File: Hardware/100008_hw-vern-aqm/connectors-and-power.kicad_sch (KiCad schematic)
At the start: 25 parts

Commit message: schematic work
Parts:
- removed D? (x2): ESD321, Diode_SMD:D_SOD-523, symbol Diode:ESD5Zxx
- added D? (x4): ESD321DYAR, Diode_SMD:D_SOD-523, symbol Active-Components:ESD321DYAR
- added R? (x2): 100R, Resistor_SMD:R_0603_1608Metric, symbol Device:R
- R?: now not fitted; now left out of the parts list
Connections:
- net GND: now also D?.2 (A), D?.2 (A), D?.2 (A), D?.2 (A)
- net UART0_RX: now also R?.2; no longer J?.2 (Pin_2)
- net UART0_TX: now also R?.2; no longer J?.1 (Pin_1)
- net at J?.A7 (D-), J?.B7 (D-), R?.1: now also D?.1 (K)
- net at J?.A6 (D+), J?.B6 (D+), R?.1: now also D?.1 (K)
- new net: D?.1 (K), J?.1 (Pin_1), R?.1
- new net: D?.1 (K), J?.2 (Pin_2), R?.1
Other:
- moved on the sheet: C?, D?, F?, J?, R?, U?

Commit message: schematic work
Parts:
- removed D?: LED, LED_SMD:LED_0805_2012Metric, symbol Device:LED
- removed J?: USB_C_Receptacle_USB2.0_16P, symbol Connector:USB_C_Receptacle_USB2.0_16P
- added D?: LED, LED_SMD:LED_0603_1608Metric, symbol Device:LED
- added J?: USB4220-03-1000-C, Mechanical:USB_C_Receptacle_GCT_USB4220-03-xxxx-C_Vertical, symbol Mechanical-Parts:GCT_USB4220-03-1000-C
- added TP? (x2): TestPoint, TestPoint:TestPoint_Pad_D1.5mm, symbol Connector:TestPoint
- D?: footprint LED_SMD:LED_0805_2012Metric -> LED_SMD:LED_0603_1608Metric
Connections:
- net +3V3: now also TP?.1
- net GND: now also D?.1 (K), J?.A1 (GND), J?.A12 (GND), J?.B1 (GND), J?.B12 (GND), J?.S1 (SHIELD)
- net VBUS: now also TP?.1
- net at R?.2: now also D?.2 (A)
- net at R?.1: now also J?.B5 (CC2)
- net at D?.1 (K), R?.1: now also J?.A7 (D-), J?.B7 (D-)
- net at D?.1 (K), R?.1: now also J?.A6 (D+), J?.B6 (D+)
- net at D?.1 (K), F?.1: now also J?.A4 (VBUS), J?.A9 (VBUS), J?.B4 (VBUS), J?.B9 (VBUS)
- net at R?.1: now also J?.A5 (CC1)
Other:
- moved on the sheet: C?, D?, F?, J?, R?, U?

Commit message: schematic work
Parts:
- added C? (x2): 10u, Capacitor_SMD:C_0805_2012Metric, symbol Device:C
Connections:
- net +3V3: now also C?.1
- net GND: now also C?.2, C?.2
- net VBUS: now also C?.1
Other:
- moved on the sheet: C?, R?, U?

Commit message: schematic and pcb work
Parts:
- added J?: Conn_01x04_Socket, symbol Connector:Conn_01x04_Socket
- added R? (x3): 10k, Resistor_SMD:R_0603_1608Metric, symbol Device:R
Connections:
- net +3V3: now also R?.1, R?.1, R?.1
- net GND: now also J?.MP (MountPin)
- new net SD_CS(D3): J?.1 (Pin_1), R?.2
- new net SD_MISO(D0): J?.3 (Pin_3), R?.2
- new net SD_MOSI(CMD): J?.2 (Pin_2), R?.2
- new net SD_SCK(CLK): J?.4 (Pin_4)
- no-connect marks 6 -> 5
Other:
- note added: "LCD Display SD card pin header connector"
- moved on the sheet: D?, J?, R?, TP?

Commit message: schematic and pcb layout
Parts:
- added J5: Conn_01x06_Socket, Connector_PinHeader_2.00mm:PinHeader_1x06_P2.00mm_Vertical, symbol Connector:Conn_01x06_Socket
- added J7: Conn_01x05_Pin, Connector_PinHeader_2.54mm:PinHeader_1x05_P2.54mm_Vertical, symbol Connector:Conn_01x05_Pin
- added R10: 0R0, Resistor_SMD:R_0603_1608Metric, symbol Device:R
- C2: renamed from C?; now not fitted
- F1: renamed from F?; footprint (none) -> Fuse:Fuse_1206_3216Metric; MFN (none) -> SN050-08
- J1: renamed from J?; footprint (none) -> Connector_PinHeader_2.54mm:PinHeader_1x14_P2.54mm_Vertical
- J4: renamed from J?; footprint (none) -> Connector_PinHeader_2.54mm:PinHeader_1x03_P2.54mm_Vertical
- J6: renamed from J?; footprint (none) -> Connector_PinHeader_2.54mm:PinHeader_1x04_P2.54mm_Vertical
- gave numbers to parts that had none: 32
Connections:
- net +3V3: no longer C5.1, C6.1
- net GND: now also J5.2 (Pin_2), J7.5 (Pin_5), R10.2
- net I2C_SCL: now also J5.4 (Pin_4)
- net I2C_SDA: now also J5.3 (Pin_3)
- net VBUS: now also J5.1 (Pin_1)
- net at R14.1, U1.2 (VO): now also C5.1, C6.1
- new net: J5.5 (Pin_5), R10.1
- new net JTAG_TCK: J7.1 (Pin_1)
- new net JTAG_TDI: J7.3 (Pin_3)
- new net JTAG_TDO: J7.2 (Pin_2)
- new net JTAG_TMS: J7.4 (Pin_4)
- no-connect marks 5 -> 6
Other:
- note added: "JTAG connector"
- moved on the sheet: C5, C6, D4, D5, D6, D7, R14, R15, R16, TP1, TP2

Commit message: schematic and pcb general layout
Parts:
- added H1, H2, H3, H4: MountingHole, MountingHole:MountingHole_4.5mm, symbol Mechanical:MountingHole
- J1, J6: now not fitted
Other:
- note added: "Mounting holes"

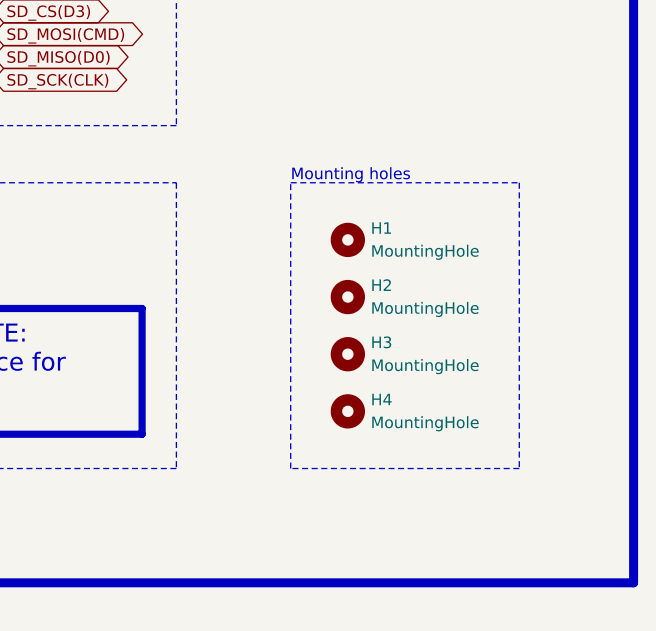
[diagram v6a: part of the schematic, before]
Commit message: schematic, pcb layout, added mouser shoping cart
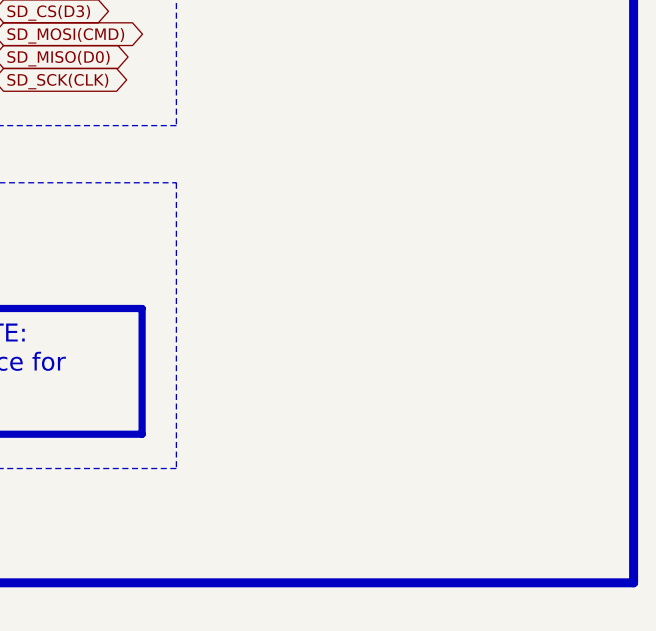
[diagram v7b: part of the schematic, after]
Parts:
- removed H1, H2, H3, H4: MountingHole, MountingHole:MountingHole_4.5mm, symbol Mechanical:MountingHole
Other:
- note removed: "Mounting holes"
